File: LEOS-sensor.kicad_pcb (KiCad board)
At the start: 2 copper layers, 100 x 100 mm, 46 parts, among them J1 MicroFit_1x4, J2 MicroFit_1x4, J3 Screw_Terminal_01x08, J4 I2C 0, J5 I2C 1, J6 SPI 1, J7 UART 0, K1 G6DN-1A DC5, K2 G6DN-1A DC5, K3 G6DN-1A DC5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

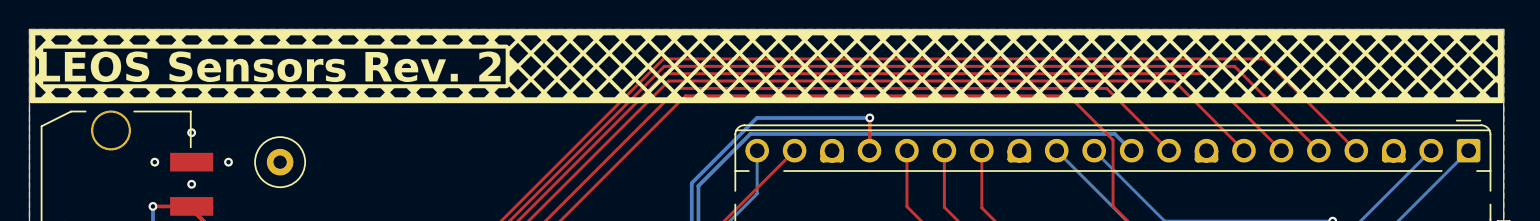
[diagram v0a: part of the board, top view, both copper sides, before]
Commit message: Add production date and up revision
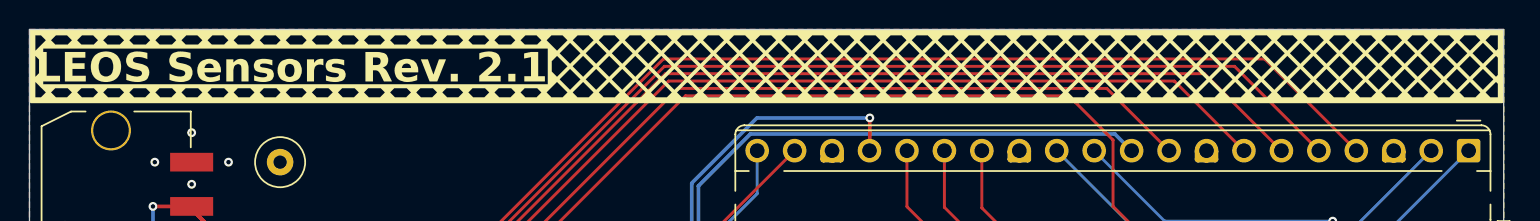
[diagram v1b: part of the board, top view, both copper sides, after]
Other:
- board text added: "02/17/2026"
- board text added: "LEOS Sensors Rev. 2.1"
- board text removed: "LEOS Sensors Rev. 2"
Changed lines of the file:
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@@
 			(drillshape 0)
 			(scaleselection 1)
-			(outputdirectory "/home/matthewlyon/Projects/LEOS-stack-template/LEOS-stack-template-rd1/")
+			(outputdirectory "./")
 		)
 	)
@@
 		)
 	)
-	(gr_text "LEOS Sensors Rev. 2"
+	(gr_text "LEOS Sensors Rev. 2.1"
 		(at 100.4 52.6 0)
 		(layer "F.SilkS" knockout)
@@
 		)
 	)
+	(gr_text "02/17/2026"
+		(at 100.75 52.5 -0)
+		(layer "B.SilkS" knockout)
+		(effects
+			(font
+				(size 2 2)
+				(thickness 0.4)
+				(bold yes)
+			)
+			(justify right mirror)
+		)
+	)
